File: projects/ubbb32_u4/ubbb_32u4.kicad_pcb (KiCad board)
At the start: 2 copper layers, 41.9 x 20.3 mm, 30 parts, among them CON1 USB-MINI-B, P1 ISP, P2 CONN_5, P3 CONN_5, P4 CONN_5, P5 CONN_5, P6 CONN_5, P7 CONN_5, SW1 SW_PUSH_SMALL, SW2 SW_PUSH_SMALL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

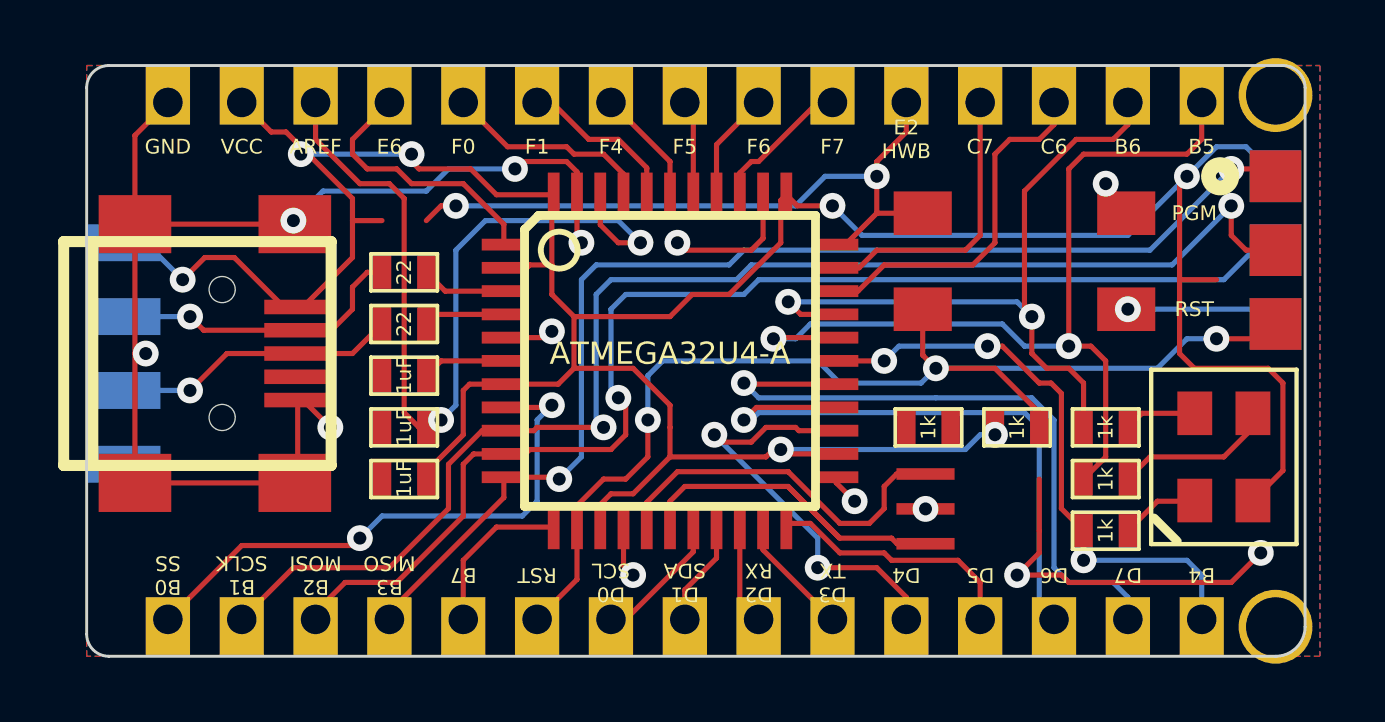
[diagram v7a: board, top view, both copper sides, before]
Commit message: Added resonator to u4 board
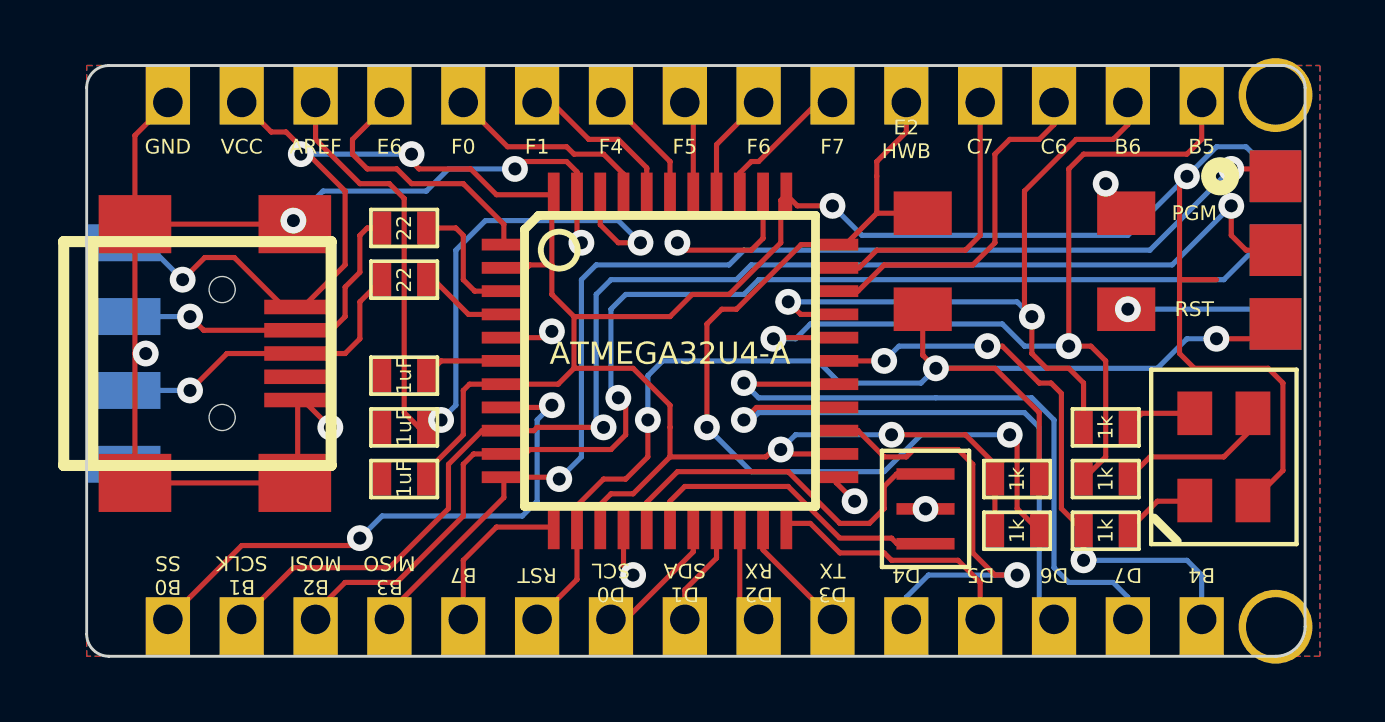
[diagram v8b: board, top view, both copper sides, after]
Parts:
- moved R6 4.68 mm to (57.1, 47.8), turned to 180 degrees
- moved R4 1.78 mm to (57.1, 46.0)
- moved R2 1.52 mm to (36.1, 39.1)
- moved R3 1.52 mm to (36.1, 37.3)
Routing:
- net (no net): track 12.5 -> 0.00 mm, vias 2 -> 0
- net /E2: track 23.8 -> 32.1 mm
- net N-0000017: track 13.2 -> 10.7 mm
- net /RESET: track 40.3 -> 42.1 mm
- net /D-: track 10.4 -> 11.9 mm
- net N-0000040: track 2.94 -> 4.46 mm
- net /D+: track 9.84 -> 11.2 mm
- net +5V: track 111.8 -> 113.0 mm
- net /D4: track 14.8 -> 15.9 mm, vias 2 -> 1
